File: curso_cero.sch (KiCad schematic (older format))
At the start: 24 parts, among them P1 Arduino Power header, P2 Arduino Analog header, P3 Analog pin, P4 Digital pin, P5 Servo 1, P6 Servo 2, P7 Arduino Digital H header, P8 Arduino Digital L header, P9 Power, SW1 SW_PUSH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

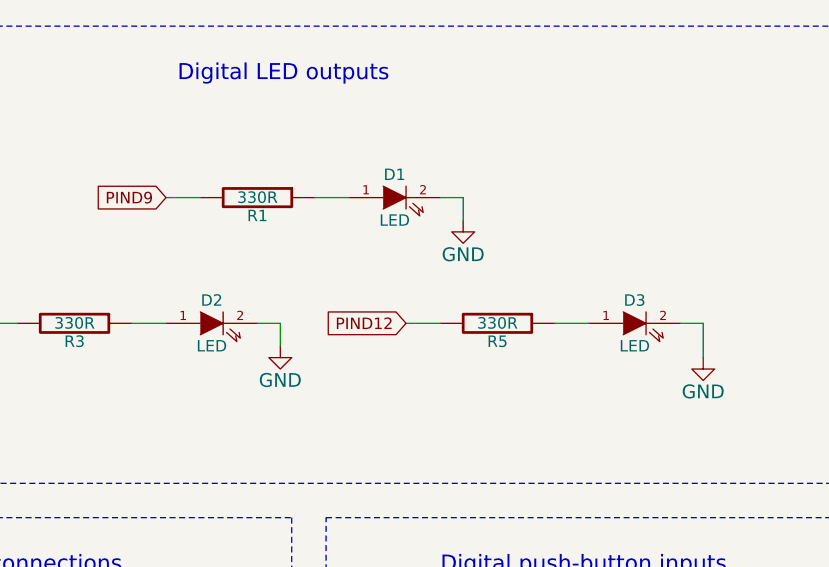
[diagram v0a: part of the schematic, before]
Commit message: añadidos valores de LED segun color
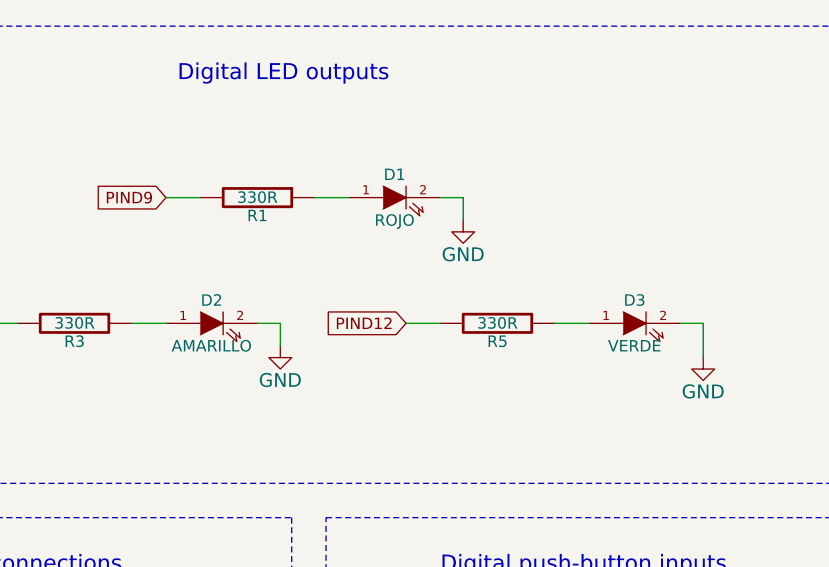
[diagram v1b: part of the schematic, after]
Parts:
- D1: value LED -> ROJO
- D2: value LED -> AMARILLO
- D3: value LED -> VERDE
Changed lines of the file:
@@
 P 2850 4100
 F 0 "D2" H 2850 4200 50  0000 C CNN
-F 1 "LED" H 2850 4000 50  0000 C CNN
+F 1 "AMARILLO" H 2850 4000 50  0000 C CNN
 F 2 "LEDs:LED_D5.0mm" H 2850 4100 60  0001 C CNN
 F 3 "" H 2850 4100 60  0000 C CNN
@@
 P 4700 4100
 F 0 "D3" H 4700 4200 50  0000 C CNN
-F 1 "LED" H 4700 4000 50  0000 C CNN
+F 1 "VERDE" H 4700 4000 50  0000 C CNN
 F 2 "LEDs:LED_D5.0mm" H 4700 4100 60  0001 C CNN
 F 3 "" H 4700 4100 60  0000 C CNN
@@
 P 3650 3550
 F 0 "D1" H 3650 3650 50  0000 C CNN
-F 1 "LED" H 3650 3450 50  0000 C CNN
+F 1 "ROJO" H 3650 3450 50  0000 C CNN
 F 2 "LEDs:LED_D5.0mm" H 3650 3550 60  0001 C CNN
 F 3 "" H 3650 3550 60  0000 C CNN
